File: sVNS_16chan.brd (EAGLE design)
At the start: 160 x 100 mm, 52 parts, among them IC1 EFM8SB10F8G-A-CSP16R, IC2 OPA990IDCKR, U1 NT3H2211W0FHKH, U2 LT8410EDC-1#TRMPBF, U3 MUX36S16IRSNR, U4 MUX36S16IRSNR

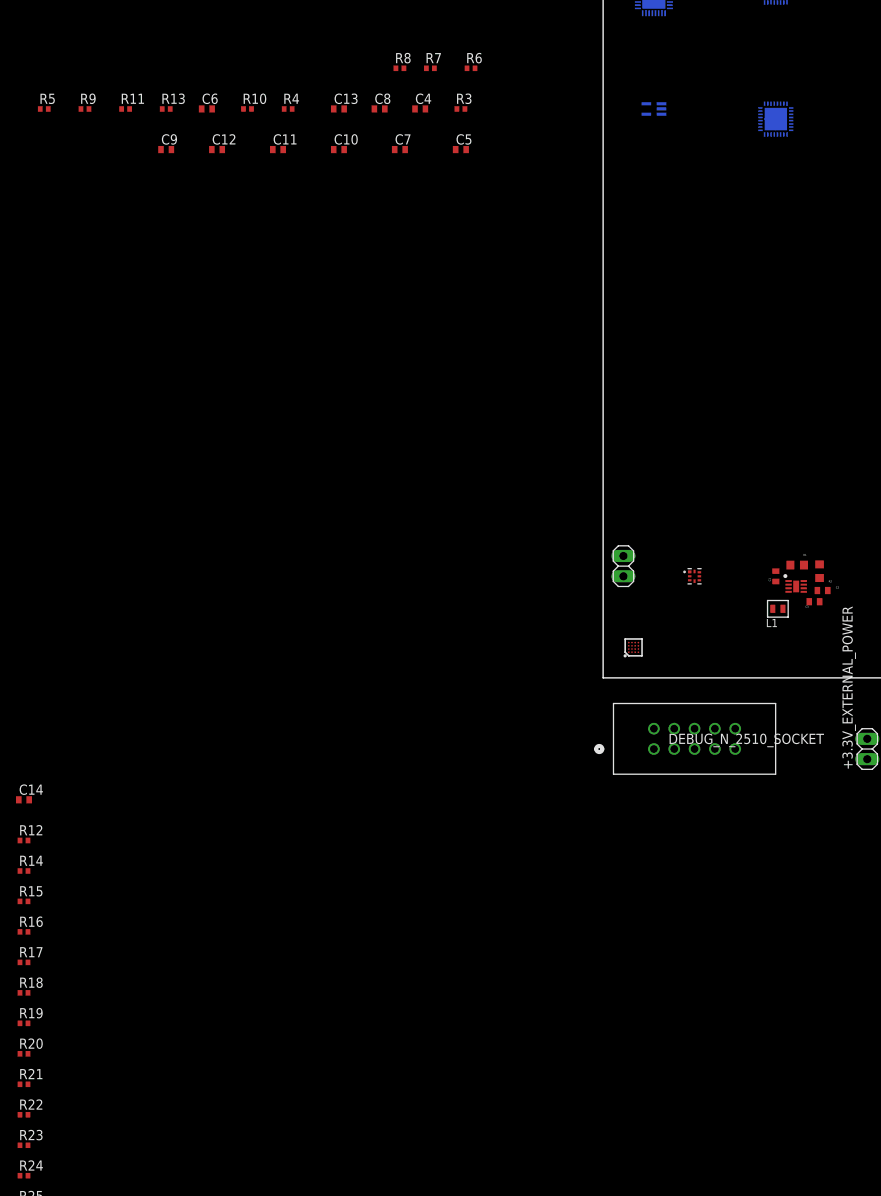
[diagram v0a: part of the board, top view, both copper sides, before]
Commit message: Setup/draft the top layer
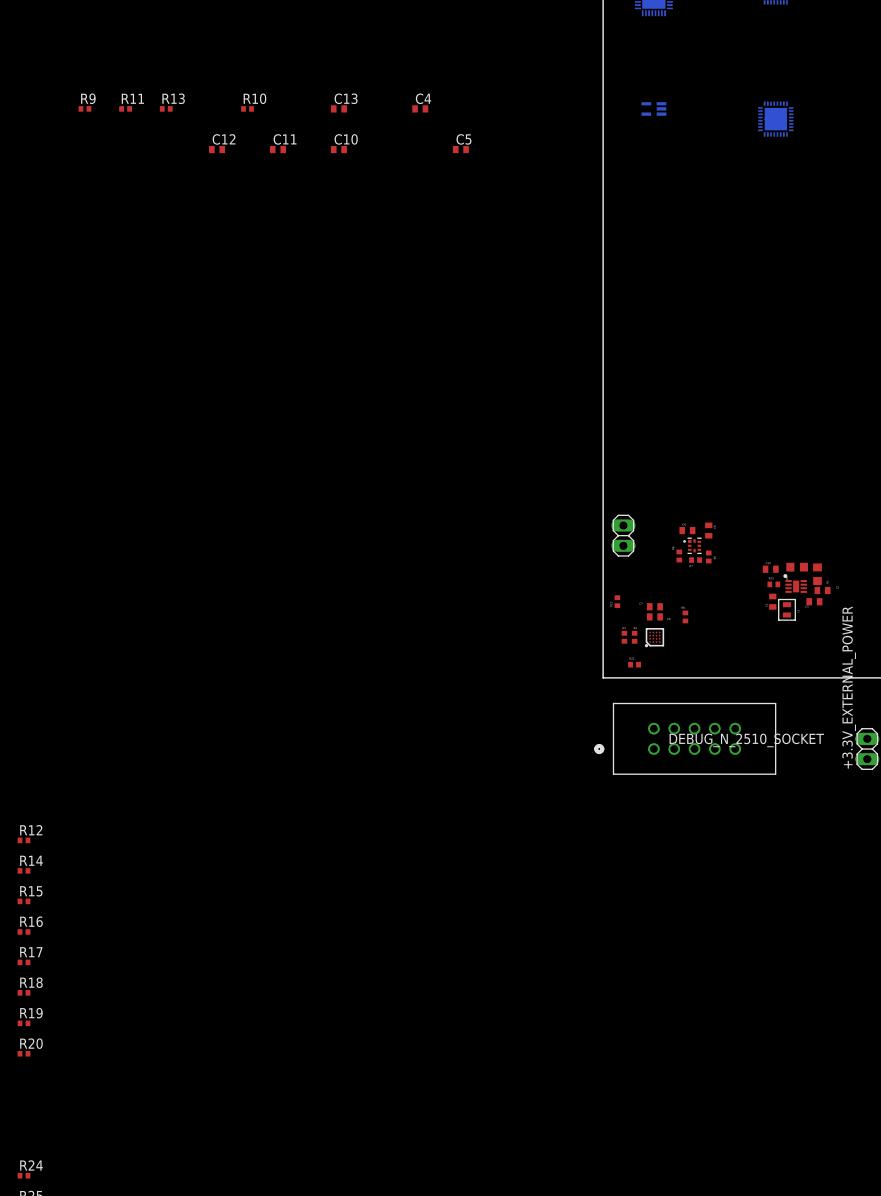
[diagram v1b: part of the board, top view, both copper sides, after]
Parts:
- moved R23 117.0 mm to (21.3, 11.7)
- moved R5 100.2 mm to (13.2, 15.1), turned to 270 degrees
- moved C14 97.7 mm to (21.0, 13.6)
- moved R21 95.6 mm to (1.78, 9.53), turned to 90 degrees
- moved R22 94.8 mm to (3.94, 1.65)
- moved C9 82.9 mm to (13.2, 18.4), turned to 270 degrees
- moved C6 79.9 mm to (10.5, 18.4)
- moved R4 79.0 mm to (3.94, 5.08), turned to 270 degrees
- moved R8 77.3 mm to (10.3, 7.62), turned to 270 degrees
- moved C8 72.2 mm to (6.48, 7.62)
- moved R7 69.8 mm to (11.6, 14.7)
- moved R3 69.1 mm to (2.67, 5.08), turned to 90 degrees
- moved R6 66.3 mm to (9.53, 15.2), turned to 270 degrees
- moved C7 65.4 mm to (6.48, 8.89), turned to 180 degrees
- moved U1 3.81 mm to (11.4, 16.5)
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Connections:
- removed net IREF: IC2.1, R9.2
- net P0.7_IREF: now also IC2.1, R9.2

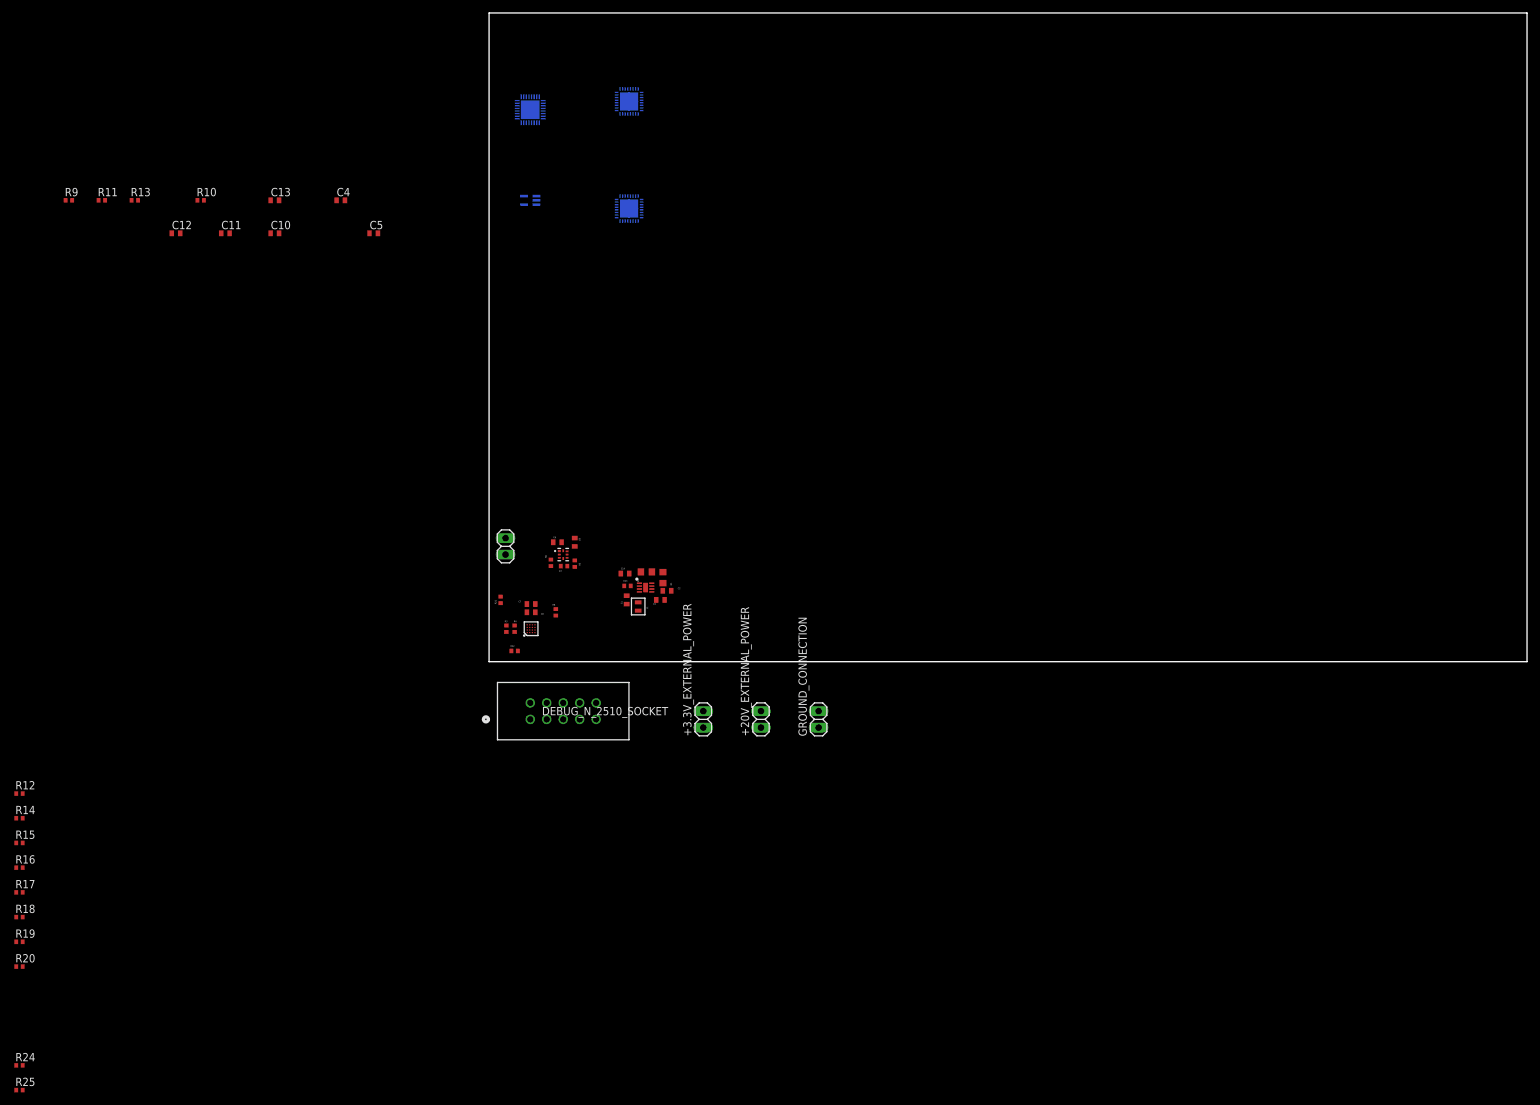
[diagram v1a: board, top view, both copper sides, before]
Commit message: Dual sided setup: components on both sides. Components grouped. No wiring yet.
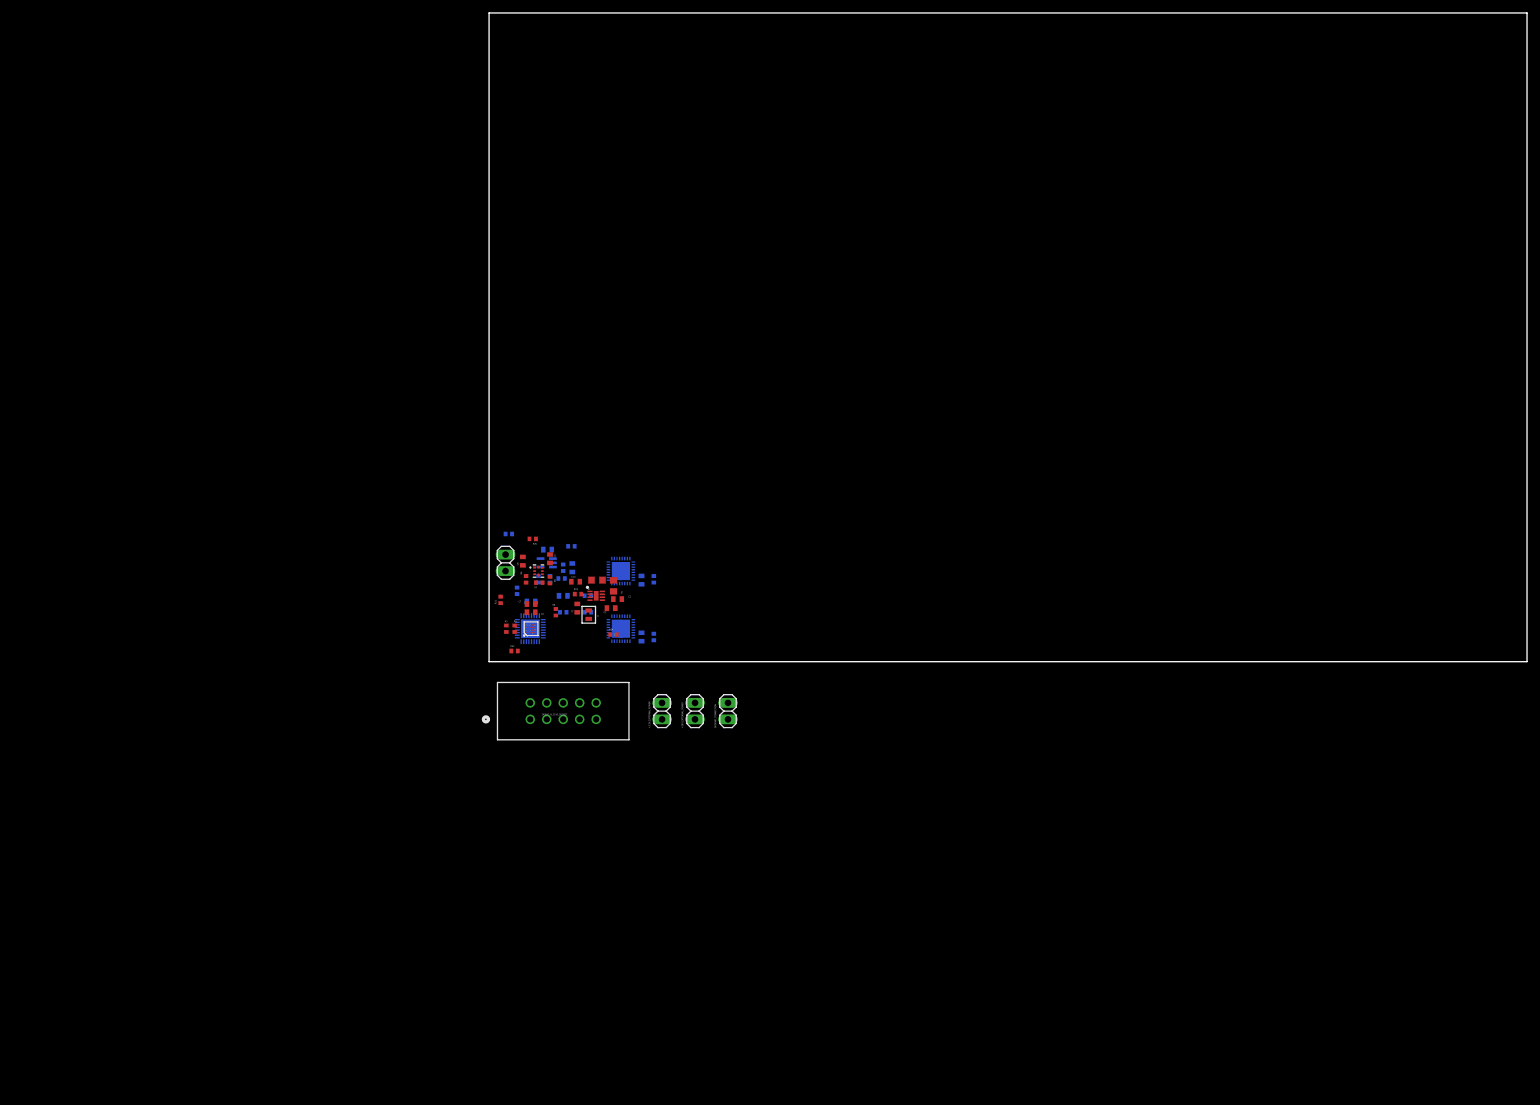
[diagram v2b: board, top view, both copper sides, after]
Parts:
- moved R25 116.1 mm to (6.73, 18.9), turned to 180 degrees
- moved R24 113.1 mm to (19.2, 4.19)
- moved R19 112.6 mm to (25.4, 12.7), flipped to the bottom, turned to 270 degrees
- moved R20 110.2 mm to (25.4, 3.81), flipped to the bottom, turned to 270 degrees
- moved R18 97.0 mm to (9.40, 12.7), flipped to the bottom, turned to 270 degrees
- moved R15 95.6 mm to (15.2, 10.2), flipped to the bottom
- moved R9 94.1 mm to (12.7, 17.8), flipped to the bottom
- moved R17 93.5 mm to (3.05, 19.7), flipped to the bottom
- moved R14 93.2 mm to (15.2, 7.62), flipped to the bottom
- moved R13 91.6 mm to (11.4, 7.62), flipped to the bottom, turned to 180 degrees
- moved R16 91.5 mm to (7.62, 12.7), flipped to the bottom, turned to 270 degrees
- moved R11 90.9 mm to (11.4, 14.5), flipped to the bottom, turned to 90 degrees
- moved R12 82.8 mm to (4.32, 10.9), flipped to the bottom, turned to 270 degrees
- moved R10 80.6 mm to (11.2, 12.8), flipped to the bottom
- moved U$1 80.0 mm to (6.35, 5.08)
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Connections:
- removed net +20V1: C12.1
- removed net GND1: C12.2
- net +3.3V: no longer U1.7
- net +3.3V_PIN: now also U1.7
- net GND: now also C12.2
- net OPAMP_+20V: now also C12.1
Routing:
- added copper zone on layer 2, net GND

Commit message: Decreased space between components. Changed the antenna connector. Ready for routing
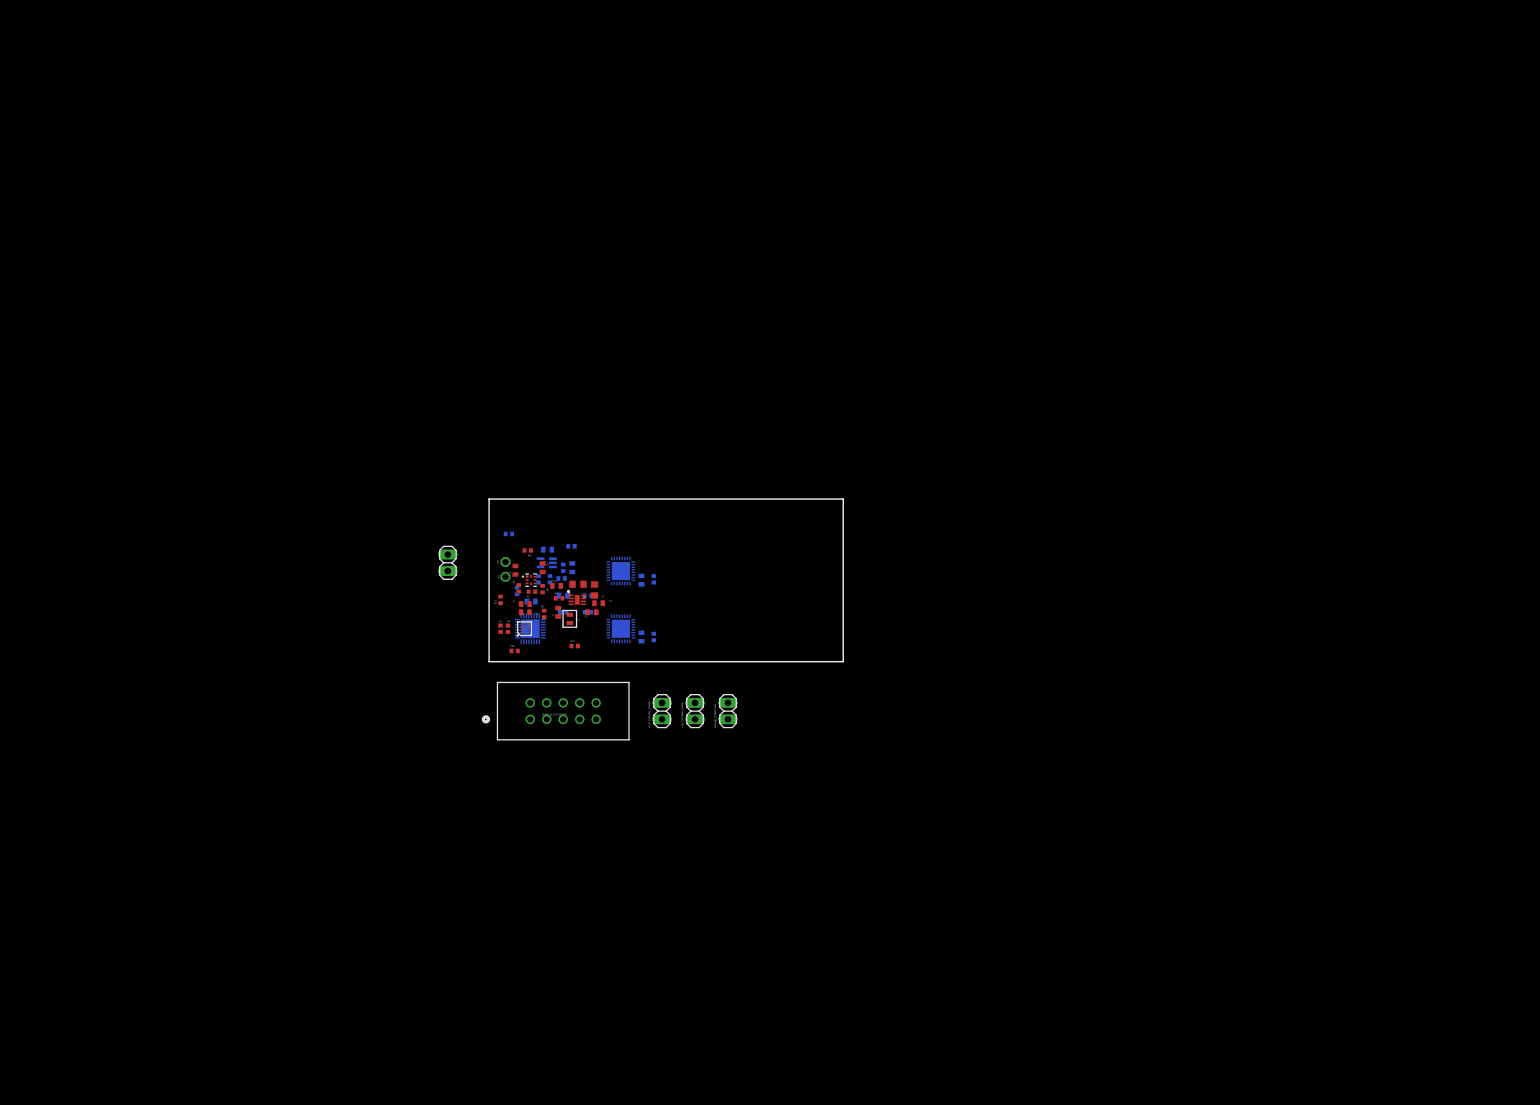
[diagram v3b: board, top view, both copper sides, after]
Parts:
- added JP1, JP2: (no value), sVNS_16chan_lib:1X01
- moved ANTENNA 8.89 mm to (-6.35, 15.2)
- moved R24 6.23 mm to (13.2, 2.41)
- moved C2 2.99 mm to (16.9, 9.02)
- moved C14 2.99 mm to (10.4, 11.7)
- moved C1 2.99 mm to (10.7, 7.62)
- moved L1 2.99 mm to (12.4, 6.60)
- moved R2 2.99 mm to (13.7, 11.9)
- moved U2 2.99 mm to (13.6, 9.53)
- moved C3 2.99 mm to (15.9, 7.62)
- moved R1 2.99 mm to (16.3, 11.0)
- moved R23 2.99 mm to (10.8, 9.78)
- moved R25 1.93 mm to (5.97, 17.1)
- moved C6 1.81 mm to (4.06, 14.1)
- moved R7 1.81 mm to (6.60, 10.8)
- moved U1 1.81 mm to (6.48, 12.6)
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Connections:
- net +20V: no longer C3.1, U2.5
- net +20V_PIN: now also C3.1, U2.5
- net LA: now also JP1.1; no longer ANTENNA.1
- net LB: now also JP2.1; no longer ANTENNA.2
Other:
- board size 160 x 100 mm -> 54.6 x 25.1 mm

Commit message: Experimentation and routing
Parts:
- moved R21 26.1 mm to (-6.35, -15.2), turned to 0 degrees
- moved R1 2.43 mm to (16.0, 8.64)
- moved C1 2.43 mm to (10.4, 5.21)
- moved C3 2.43 mm to (15.6, 5.21)
- moved L1 2.43 mm to (12.2, 4.19)
- moved R2 2.43 mm to (13.5, 9.53)
- moved R23 2.43 mm to (10.5, 7.37)
- moved U2 2.43 mm to (13.3, 7.11)
- moved C2 2.43 mm to (16.6, 6.60)
- moved C14 2.43 mm to (10.2, 9.27)
- moved R24 2.25 mm to (15.4, 1.78)
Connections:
- net +3.3V: no longer C7.2, C8.1, R8.1
- net +3.3V_VDD: now also C7.2, C8.1, R8.1

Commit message: Experimentation and routing
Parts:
- added J1: TSM-130-01-F-SV, TSM-130-01-F-SV:SAMTEC_TSM-130-01-F-SV
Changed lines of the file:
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@@
 <layers>
 <layer number="1" name="Top" color="4" fill="1" visible="yes" active="yes"/>
-<layer number="2" name="Route2(GND)" color="16" fill="1" visible="no" active="yes"/>
+<layer number="2" name="Route2(GND)" color="16" fill="1" visible="yes" active="yes"/>
 <layer number="3" name="Route3" color="17" fill="1" visible="no" active="no"/>
 <layer number="4" name="Route4" color="18" fill="1" visible="no" active="no"/>
@@
 <layer number="13" name="Route13" color="21" fill="1" visible="no" active="no"/>
 <layer number="14" name="Route14" color="22" fill="1" visible="no" active="no"/>
-<layer number="15" name="Route15(power)" color="23" fill="1" visible="no" active="yes"/>
-<layer number="16" name="Bottom" color="1" fill="1" visible="no" active="yes"/>
+<layer number="15" name="Route15(power)" color="23" fill="1" visible="yes" active="yes"/>
+<layer number="16" name="Bottom" color="1" fill="1" visible="yes" active="yes"/>
 <layer number="17" name="Pads" color="2" fill="1" visible="yes" active="yes"/>
 <layer number="18" name="Vias" color="2" fill="1" visible="yes" active="yes"/>
@@
 <layer number="20" name="Dimension" color="24" fill="1" visible="yes" active="yes"/>
 <layer number="21" name="tPlace" color="7" fill="1" visible="yes" active="yes"/>
-<layer number="22" name="bPlace" color="7" fill="1" visible="no" active="yes"/>
+<layer number="22" name="bPlace" color="7" fill="1" visible="yes" active="yes"/>
 <layer number="23" name="tOrigins" color="15" fill="1" visible="yes" active="yes"/>
-<layer number="24" name="bOrigins" color="15" fill="1" visible="no" active="yes"/>
+<layer number="24" name="bOrigins" color="15" fill="1" visible="yes" active="yes"/>
 <layer number="25" name="tNames" color="7" fill="1" visible="yes" active="yes"/>
-<layer number="26" name="bNames" color="7" fill="1" visible="no" active="yes"/>
+<layer number="26" name="bNames" color="7" fill="1" visible="yes" active="yes"/>
 <layer number="27" name="tValues" color="7" fill="1" visible="no" active="yes"/>
 <layer number="28" name="bValues" color="7" fill="1" visible="no" active="yes"/>
@@
 <layer number="38" name="bTest" color="7" fill="1" visible="no" active="yes"/>
 <layer number="39" name="tKeepout" color="4" fill="11" visible="yes" active="yes"/>
-<layer number="40" name="bKeepout" color="1" fill="11" visible="no" active="yes"/>
+<layer number="40" name="bKeepout" color="1" fill="11" visible="yes" active="yes"/>
 <layer number="41" name="tRestrict" color="4" fill="10" visible="yes" active="yes"/>
-<layer number="42" name="bRestrict" color="1" fill="10" visible="no" active="yes"/>
+<layer number="42" name="bRestrict" color="1" fill="10" visible="yes" active="yes"/>
 <layer number="43" name="vRestrict" color="2" fill="10" visible="no" active="yes"/>
 <layer number="44" name="Drills" color="7" fill="1" visible="no" active="yes"/>
@@
 <layer number="50" name="dxf" color="7" fill="1" visible="no" active="no"/>
 <layer number="51" name="tDocu" color="7" fill="1" visible="yes" active="yes"/>
-<layer number="52" name="bDocu" color="7" fill="1" visible="no" active="yes"/>
+<layer number="52" name="bDocu" color="7" fill="1" visible="yes" active="yes"/>
 <layer number="53" name="tGND_GNDA" color="7" fill="9" visible="no" active="no"/>
 <layer number="54" name="bGND_GNDA" color="1" fill="9" visible="no" active="no"/>
@@
 <attribute name="VALUE" x="-6.985" y="-17.145" size="1.27" layer="27"/>
 </element>
+<element name="J1" library="TSM-130-01-F-SV" package="SAMTEC_TSM-130-01-F-SV" value="TSM-130-01-F-SV" x="31.75" y="-22.86" smashed="yes">
+<attribute name="MANUFACTURER" value="SAMTEC " x="31.75" y="-22.86" size="1.778" layer="27" display="off"/>
+<attribute name="NAME" x="-6.35" y="-18.67" size="1.27" layer="25"/>
+<attribute name="VALUE" x="-6.35" y="-28.3" size="1.27" layer="27"/>
+</element>
 </elements>
